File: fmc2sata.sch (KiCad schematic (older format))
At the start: 40 parts, among them J1 ASP-134488-01, J2 1-2199230-6, J3 te-770829-1, U1 TPS565208, U2 TPS565208, Y1 AX3DAF1-150.0000

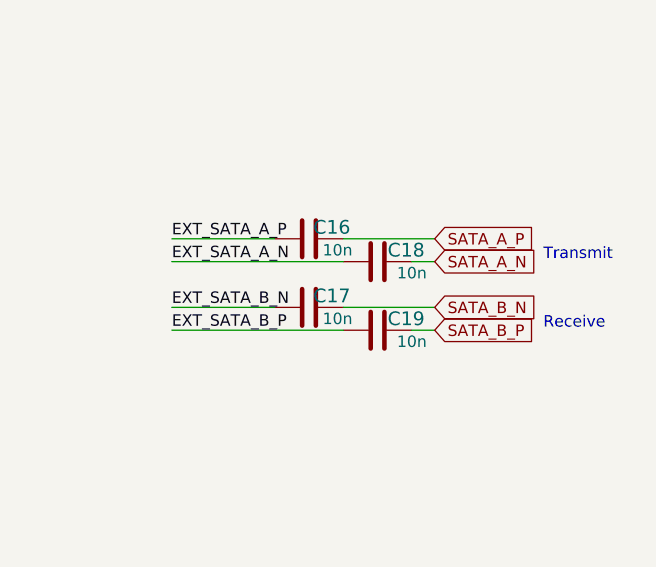
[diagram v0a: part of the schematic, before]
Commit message: Add board fastening holes
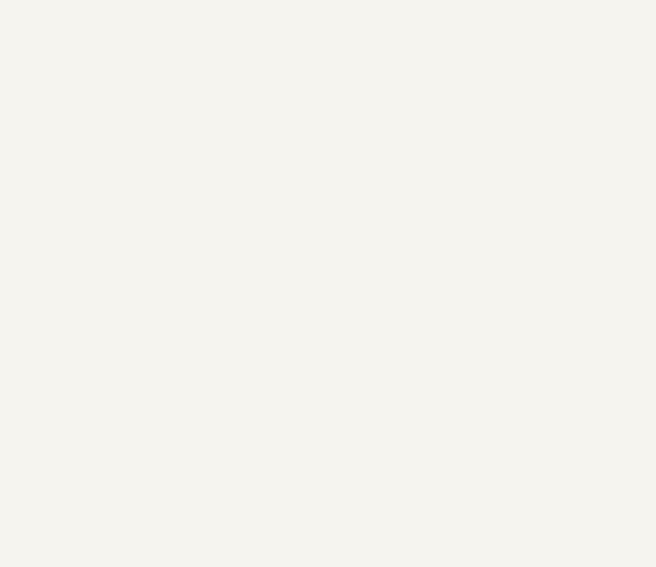
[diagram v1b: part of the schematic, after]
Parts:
- removed C16, C17, C18, C19: C_10n_0402, antmicro-footprints:0402-cap, symbol antmicroCapacitors0402:C_10n_0402
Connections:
- net labels removed: EXT_SATA_A_N, EXT_SATA_A_P, EXT_SATA_B_N, EXT_SATA_B_P
- wire segments 268 -> 260
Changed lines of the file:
@@
 Text Label 10650 4525 0    50   ~ 0
 M2_SATA_B_P
-Text GLabel 14900 5550 2    50   Input ~ 0
-SATA_B_P
-Text GLabel 14900 5450 2    50   Input ~ 0
-SATA_B_N
-Text Notes 15375 5550 0    50   ~ 0
-Receive
-Wire Wire Line
-	14200 5450 13750 5450
-Wire Wire Line
-	14800 5550 14900 5550
-Wire Wire Line
-	14500 5450 14900 5450
-Wire Wire Line
-	13750 5550 14500 5550
-$Comp
-L antmicroCapacitors0402:C_10n_0402 C19
-U 1 1 603C8A00
-P 14650 5550
-F 0 "C19" V 14600 5675 60  0000 C CNN
-F 1 "C_10n_0402" H 14650 5400 60  0001 C CNN
-F 2 "antmicro-footprints:0402-cap" H 14850 5750 60  0001 L CNN
-F 3 "" H 14650 5550 50  0001 C CNN
-F 4 "AVX" H 14850 5950 60  0001 L CNN "Manufacturer"
-F 5 "04025G103ZAT2A" H 14850 5850 60  0001 L CNN "MPN"
-F 6 "10n" V 14700 5700 50  0000 C CNN "Val"
-	1    14650 5550
-	0    1    1    0
-$EndComp
-$Comp
-L antmicroCapacitors0402:C_10n_0402 C17
-U 1 1 603C8A09
-P 14350 5450
-F 0 "C17" V 14300 5550 60  0000 C CNN
-F 1 "C_10n_0402" H 14350 5300 60  0001 C CNN
-F 2 "antmicro-footprints:0402-cap" H 14550 5650 60  0001 L CNN
-F 3 "" H 14350 5450 50  0001 C CNN
-F 4 "AVX" H 14550 5850 60  0001 L CNN "Manufacturer"
-F 5 "04025G103ZAT2A" H 14550 5750 60  0001 L CNN "MPN"
-F 6 "10n" V 14400 5575 50  0000 C CNN "Val"
-	1    14350 5450
-	0    1    1    0
-$EndComp
-Text Notes 15375 5250 0    50   ~ 0
-Transmit
-Wire Wire Line
-	14800 5250 14900 5250
-Wire Wire Line
-	14500 5150 14900 5150
-Wire Wire Line
-	13750 5250 14500 5250
-$Comp
-L antmicroCapacitors0402:C_10n_0402 C18
-U 1 1 603C8A16
-P 14650 5250
-F 0 "C18" V 14600 5375 60  0000 C CNN
-F 1 "C_10n_0402" H 14650 5100 60  0001 C CNN
-F 2 "antmicro-footprints:0402-cap" H 14850 5450 60  0001 L CNN
-F 3 "" H 14650 5250 50  0001 C CNN
-F 4 "AVX" H 14850 5650 60  0001 L CNN "Manufacturer"
-F 5 "04025G103ZAT2A" H 14850 5550 60  0001 L CNN "MPN"
-F 6 "10n" V 14700 5400 50  0000 C CNN "Val"
-	1    14650 5250
-	0    1    1    0
-$EndComp
-$Comp
-L antmicroCapacitors0402:C_10n_0402 C16
-U 1 1 603C8A1F
-P 14350 5150
-F 0 "C16" V 14300 5250 60  0000 C CNN
-F 1 "C_10n_0402" H 14350 5000 60  0001 C CNN
-F 2 "antmicro-footprints:0402-cap" H 14550 5350 60  0001 L CNN
-F 3 "" H 14350 5150 50  0001 C CNN
-F 4 "AVX" H 14550 5550 60  0001 L CNN "Manufacturer"
-F 5 "04025G103ZAT2A" H 14550 5450 60  0001 L CNN "MPN"
-F 6 "10n" V 14400 5275 50  0000 C CNN "Val"
-	1    14350 5150
-	0    1    1    0
-$EndComp
-Text GLabel 14900 5150 2    50   Input ~ 0
-SATA_A_P
-Text GLabel 14900 5250 2    50   Input ~ 0
-SATA_A_N
-Wire Wire Line
-	13750 5150 14200 5150
-Text Label 13750 5150 0    50   ~ 0
-EXT_SATA_A_P
-Text Label 13750 5250 0    50   ~ 0
-EXT_SATA_A_N
-Text Label 13750 5450 0    50   ~ 0
-EXT_SATA_B_N
-Text Label 13750 5550 0    50   ~ 0
-EXT_SATA_B_P
 $Comp
 L antmicroPCConnectors:te-770829-1 J3

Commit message: Add second M.2 mouting stud
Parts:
- added N1: antmicro_logo, antmicro-footprints:antmicro-logo, symbol antmicroMechanicalParts:antmicro_logo
- added N2: oshw_logo, antmicro-footprints:oshw-logo, symbol antmicroMechanicalParts:oshw_logo
- added SP2: 9774025151, antmicro-footprints:9774025151, symbol antmicroMechanicalParts:9774025151
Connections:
- wire segments 260 -> 262
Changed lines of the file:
@@
 L power:GND #PWR01
 U 1 1 6009AC9F
-P 9325 7650
-F 0 "#PWR01" H 9325 7400 50  0001 C CNN
-F 1 "GND" H 9330 7477 50  0000 C CNN
-F 2 "" H 9325 7650 50  0001 C CNN
-F 3 "" H 9325 7650 50  0001 C CNN
-	1    9325 7650
+P 9325 7875
+F 0 "#PWR01" H 9325 7625 50  0001 C CNN
+F 1 "GND" H 9330 7702 50  0000 C CNN
+F 2 "" H 9325 7875 50  0001 C CNN
+F 3 "" H 9325 7875 50  0001 C CNN
+	1    9325 7875
 	1    0    0    -1
 $EndComp
@@
 	9400 7500 9325 7500
 Wire Wire Line
-	9325 7500 9325 7650
+	9325 7500 9325 7825
 Text Notes 13700 2425 0    79   ~ 16
 2.5" Drive Power Connector
@@
 Wire Wire Line
 	13450 3300 13450 3150
+$Comp
+L antmicroMechanicalParts:9774025151 SP2
+U 1 1 601E6B56
+P 9600 7825
+F 0 "SP2" H 9730 7878 60  0000 L CNN
+F 1 "9774025151" H 9730 7772 60  0000 L CNN
+F 2 "antmicro-footprints:9774025151" H 9600 7825 60  0001 C CNN
+F 3 "" H 9600 7825 60  0001 C CNN
+F 4 "Wurth Elektronik" H 9600 7825 50  0001 C CNN "Manufacturer"
+F 5 "9774025151" H 9600 7825 50  0001 C CNN "MPN"
+	1    9600 7825
+	1    0    0    -1
+$EndComp
+Wire Wire Line
+	9400 7825 9325 7825
+Connection ~ 9325 7825
+Wire Wire Line
+	9325 7825 9325 7875
+$Comp
+L antmicroMechanicalParts:oshw_logo N2
+U 1 1 6021D7FF
+P 15225 9575
+F 0 "N2" H 15419 9578 50  0000 L CNN
+F 1 "oshw_logo" H 15419 9487 50  0000 L CNN
+F 2 "antmicro-footprints:oshw-logo" H 15245 9335 50  0001 C CNN
+F 3 "" H 15225 9575 50  0001 C CNN
+	1    15225 9575
+	1    0    0    -1
+$EndComp
+$Comp
+L antmicroMechanicalParts:antmicro_logo N1
+U 1 1 6021EA88
+P 14325 9700
+F 0 "N1" H 14539 9793 50  0000 L CNN
+F 1 "antmicro_logo" H 14539 9702 50  0000 L CNN
+F 2 "antmicro-footprints:antmicro-logo" H 14225 9950 50  0001 C CNN
+F 3 "" H 14325 10050 50  0001 C CNN
+	1    14325 9700
+	1    0    0    -1
+$EndComp
 $EndSCHEMATC

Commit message: Add PWR indicators
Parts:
- removed R10: R_1k_0402, antmicro-footprints:0402-res, symbol antmicroResistors0402:R_1k_0402
- added D2: LTST-C191KRKT, antmicro-footprints:LED_0603, symbol antmicroLEDIndicationDiscrete:LTST-C191KRKT
- added D3, D4, D5: KP-1608CGCK, antmicro-footprints:LED_0603, symbol antmicroLEDIndicationDiscrete:KP-1608CGCK
- added Q1, Q2, Q4: BSS138APW, antmicro-footprints:SC70-3, symbol antmicroTransistorsFETsMOSFETsSingle:BSS138APW
- added Q3: DMG2305UX-13, antmicro-footprints:SOT-23-3, symbol antmicroTransistorsFETsMOSFETsSingle:DMG2305UX-13
- added R10, R14, R15, R20: R_10k_0402, antmicro-footprints:0402-res, symbol antmicroResistors0402:R_10k_0402
- added R12, R13, R21, R22: R_0R_0402, antmicro-footprints:0402-res, symbol antmicroResistors0402:R_0R_0402
- added R16, R17, R18, R19: R_330R_0402, antmicro-footprints:0402-res, symbol antmicroResistors0402:R_330R_0402
- N1: footprint antmicro-footprints:antmicro-logo -> antmicro-footprints:antmicro-logo_scaled_20mm
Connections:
- net labels added: JTAG_TDI, JTAG_TDO, PRSNT, VCC_IO
- wire segments 262 -> 295
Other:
- note added: "JTAG loop"
- note added: "LED indicators"
- note added: "Signage"
- note added: "VADJ"
- moved on the sheet: C1, C10, C11, C12, C13, C14, C15, C2, C3, C4, C5, C6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

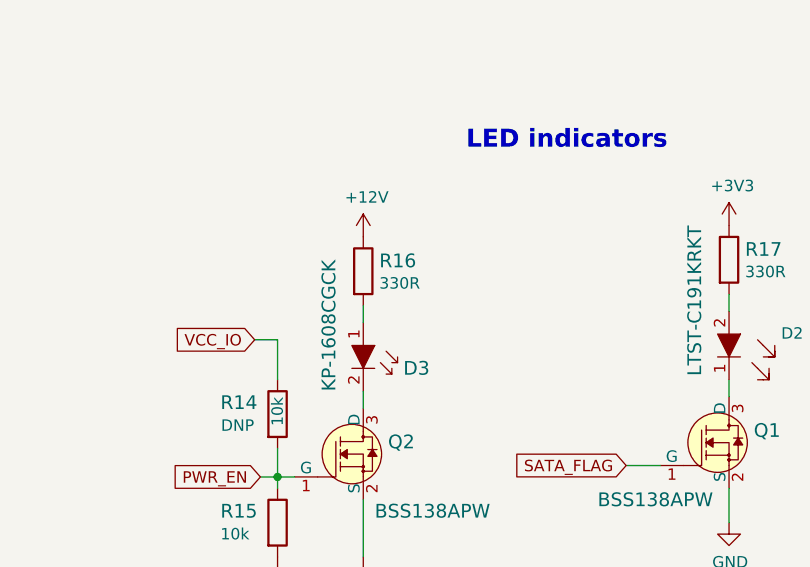
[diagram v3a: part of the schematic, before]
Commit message: Update compoent placement
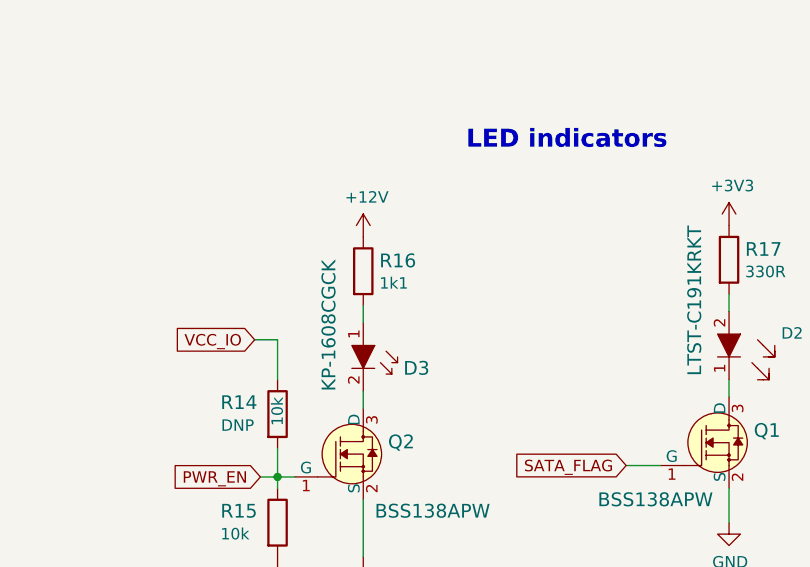
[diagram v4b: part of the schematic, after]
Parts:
- removed R16: R_330R_0402, antmicro-footprints:0402-res, symbol antmicroResistors0402:R_330R_0402
- added R16: R_1k1_0402, antmicro-footprints:0402-res, symbol antmicroResistors0402:R_1k1_0402
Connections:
- net +12V: now also R16.1
- net at D3.1: now also R16.2
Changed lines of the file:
@@
 Wire Wire Line
 	12350 6825 12350 7075
-$Comp
-L antmicroResistors0402:R_330R_0402 R16
-U 1 1 6042387E
-P 12350 5825
-F 0 "R16" V 12305 5895 60  0000 L CNN
-F 1 "R_330R_0402" H 12350 5675 60  0001 C CNN
-F 2 "antmicro-footprints:0402-res" H 12550 6025 60  0001 L CNN
-F 3 "" H 12350 5825 50  0001 C CNN
-F 4 "MULTICOMP" H 12550 6225 60  0001 L CNN "Manufacturer"
-F 5 "MCMR04X3300FTL" H 12550 6125 60  0001 L CNN "MPN"
-F 6 "330R" V 12403 5895 50  0000 L CNN "Val"
-	1    12350 5825
-	0    1    1    0
-$EndComp
 Wire Wire Line
 	12350 5975 12350 6050
@@
 Text Notes 3100 5575 0    39   ~ 0
 JTAG loop
+$Comp
+L antmicroResistors0402:R_1k1_0402 R16
+U 1 1 608DD822
+P 12350 5825
+F 0 "R16" V 12305 5895 60  0000 L CNN
+F 1 "R_1k1_0402" H 12350 5675 60  0001 C CNN
+F 2 "antmicro-footprints:0402-res" H 12550 6025 60  0001 L CNN
+F 3 "" H 12350 5825 50  0001 C CNN
+F 4 "PANASONIC_ELECTRONIC_COMPONENTS" H 12550 6225 60  0001 L CNN "Manufacturer"
+F 5 "ERJ2RKF1101X" H 12550 6125 60  0001 L CNN "MPN"
+F 6 "1k1" V 12403 5895 50  0000 L CNN "Val"
+	1    12350 5825
+	0    1    1    0
+$EndComp
 $EndSCHEMATC

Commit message: Component cleanup
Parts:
- C1, C2, C6, C7: footprint antmicro-footprints:0603-cap -> fmc2sata-footprints:0603-cap; symbol antmicroCapacitors0603:C_10u_25V_0603 -> fmc2sata:C_10u_25V_0603
- C10, C4, C5, C9: footprint antmicro-footprints:0805-cap -> fmc2sata-footprints:0805-cap; symbol antmicroCapacitorsmisc:C_22u_0805_10V -> fmc2sata:C_22u_0805_10V
- C3, C8: footprint antmicro-footprints:0603-cap -> fmc2sata-footprints:0603-cap; symbol antmicroCapacitors0603:C_100n_0603 -> fmc2sata:C_100n_0603
- D1, D3, D4, D5: footprint antmicro-footprints:LED_0603 -> fmc2sata-footprints:LED_0603; symbol antmicroLEDIndicationDiscrete:KP-1608CGCK -> fmc2sata:KP-1608CGCK
- D2: footprint antmicro-footprints:LED_0603 -> fmc2sata-footprints:LED_0603; symbol antmicroLEDIndicationDiscrete:LTST-C191KRKT -> fmc2sata:LTST-C191KRKT
- J1: footprint antmicro-footprints:ASP-134488-01 -> fmc2sata-footprints:ASP-134488-01; symbol antmicroFMCConnectors:ASP-134488-01 -> fmc2sata:ASP-134488-01
- J2: footprint antmicro-footprints:1-2199230-6 -> fmc2sata-footprints:1-2199230-6; symbol antmicroPciConnectors:1-2199230-6 -> fmc2sata:1-2199230-6
- J3: footprint antmicro-footprints:te-770829-1 -> fmc2sata-footprints:te-770829-1; symbol antmicroPCConnectors:te-770829-1 -> fmc2sata:te-770829-1
- L1: footprint antmicro-footprints:WE_74437336022 -> fmc2sata-footprints:WE_74437336022; symbol antmicroFixedInductors:WE_74437336022 -> fmc2sata:WE_74437336022
- L2: footprint antmicro-footprints:WE_74437336033 -> fmc2sata-footprints:WE_74437336033; symbol antmicroFixedInductors:WE_74437336033 -> fmc2sata:WE_74437336033
- N1: footprint antmicro-footprints:antmicro-logo_scaled_20mm -> fmc2sata-footprints:antmicro-logo_scaled_20mm; symbol antmicroMechanicalParts:antmicro_logo -> fmc2sata:antmicro_logo
- N2: footprint antmicro-footprints:oshw-logo -> fmc2sata-footprints:oshw-logo; symbol antmicroMechanicalParts:oshw_logo -> fmc2sata:oshw_logo
- Q1, Q2, Q4: footprint antmicro-footprints:SC70-3 -> fmc2sata-footprints:SC70-3; symbol antmicroTransistorsFETsMOSFETsSingle:BSS138APW -> fmc2sata:BSS138APW
- Q3: footprint antmicro-footprints:SOT-23-3 -> fmc2sata-footprints:SOT-23-3; symbol antmicroTransistorsFETsMOSFETsSingle:DMG2305UX-13 -> fmc2sata:DMG2305UX-13
- R1: footprint antmicro-footprints:0402-res -> fmc2sata-footprints:0402-res; symbol antmicroResistors0402:R_33k2_0402 -> fmc2sata:R_33k2_0402
- R11: footprint antmicro-footprints:0402-res -> fmc2sata-footprints:0402-res; symbol antmicroResistors0402:R_100R_0402 -> fmc2sata:R_100R_0402
- R12, R13, R21, R22, R3, R7, R9: footprint antmicro-footprints:0402-res -> fmc2sata-footprints:0402-res; symbol antmicroResistors0402:R_0R_0402 -> fmc2sata:R_0R_0402
- R17, R18, R19, R6: footprint antmicro-footprints:0402-res -> fmc2sata-footprints:0402-res; symbol antmicroResistors0402:R_330R_0402 -> fmc2sata:R_330R_0402
- R4: footprint antmicro-footprints:0402-res -> fmc2sata-footprints:0402-res; symbol antmicroResistors0402:R_54k9_0402 -> fmc2sata:R_54k9_0402
- SP1, SP2: footprint antmicro-footprints:9774025151 -> fmc2sata-footprints:9774025151; symbol antmicroMechanicalParts:9774025151 -> fmc2sata:9774025151
- U1, U2: footprint antmicro-footprints:SOT-23-6 -> fmc2sata-footprints:SOT-23-6; symbol antmicroPMICVoltageRegulatorsDCDCSwitchingRegulators:TPS565208 -> fmc2sata:TPS565208
- Y1: footprint antmicro-footprints:AX3DAF1 -> fmc2sata-footprints:AX3DAF1; symbol antmicroOscillators:AX3DAF1-150.0000 -> fmc2sata:AX3DAF1-150.0000

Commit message: Update local libraries
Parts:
- C11: footprint antmicro-footprints:0402-cap -> fmc2sata-footprints:0402-cap; symbol antmicroCapacitors0402:C_100n_0402 -> fmc2sata:C_100n_0402
- C12, C13, C14, C15: footprint antmicro-footprints:0402-cap -> fmc2sata-footprints:0402-cap; symbol antmicroCapacitors0402:C_10n_0402 -> fmc2sata:C_10n_0402
- R10, R14, R15, R2, R20, R5, R8: footprint antmicro-footprints:0402-res -> fmc2sata-footprints:0402-res; symbol antmicroResistors0402:R_10k_0402 -> fmc2sata:R_10k_0402
- R16: footprint antmicro-footprints:0402-res -> fmc2sata-footprints:0402-res; symbol antmicroResistors0402:R_1k1_0402 -> fmc2sata:R_1k1_0402
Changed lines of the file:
@@
 Connection ~ 9925 3950
 $Comp
-L antmicroResistors0402:R_10k_0402 R8
+L fmc2sata:R_10k_0402 R8
 U 1 1 60081456
 P 10125 3025
 F 0 "R8" V 10080 3095 60  0000 L CNN
 F 1 "R_10k_0402" H 10125 2875 60  0001 C CNN
-F 2 "antmicro-footprints:0402-res" H 10325 3225 60  0001 L CNN
+F 2 "fmc2sata-footprints:0402-res" H 10325 3225 60  0001 L CNN
 F 3 "" H 10125 3025 50  0001 C CNN
 F 4 "VISHAY" H 10325 3425 60  0001 L CNN "Manufacturer"
@@
 $EndComp
 $Comp
-L antmicroResistors0402:R_10k_0402 R2
+L fmc2sata:R_10k_0402 R2
 U 1 1 6043BD03
 P 3600 9925
 F 0 "R2" V 3555 9995 60  0000 L CNN
 F 1 "R_10k_0402" H 3600 9775 60  0001 C CNN
-F 2 "antmicro-footprints:0402-res" H 3800 10125 60  0001 L CNN
+F 2 "fmc2sata-footprints:0402-res" H 3800 10125 60  0001 L CNN
 F 3 "" H 3600 9925 50  0001 C CNN
 F 4 "VISHAY" H 3800 10325 60  0001 L CNN "Manufacturer"
@@
 $EndComp
 $Comp
-L antmicroResistors0402:R_10k_0402 R5
+L fmc2sata:R_10k_0402 R5
 U 1 1 604BD594
 P 7900 9925
 F 0 "R5" V 7855 9995 60  0000 L CNN
 F 1 "R_10k_0402" H 7900 9775 60  0001 C CNN
-F 2 "antmicro-footprints:0402-res" H 8100 10125 60  0001 L CNN
+F 2 "fmc2sata-footprints:0402-res" H 8100 10125 60  0001 L CNN
 F 3 "" H 7900 9925 50  0001 C CNN
 F 4 "VISHAY" H 8100 10325 60  0001 L CNN "Manufacturer"
@@
 	10625 9675 10625 9775
 $Comp
-L antmicroCapacitors0402:C_100n_0402 C11
+L fmc2sata:C_100n_0402 C11
 U 1 1 601CBF20
 P 10050 9600
 F 0 "C11" H 9725 9675 60  0000 L CNN
 F 1 "C_100n_0402" H 10050 9450 60  0001 C CNN
-F 2 "antmicro-footprints:0402-cap" H 10250 9800 60  0001 L CNN
+F 2 "fmc2sata-footprints:0402-cap" H 10250 9800 60  0001 L CNN
 F 3 "" H 10050 9600 50  0001 C CNN
 F 4 "Walsin" H 10250 10000 60  0001 L CNN "Manufacturer"
@@
 	9750 4450 10750 4450
 $Comp
-L antmicroCapacitors0402:C_10n_0402 C15
+L fmc2sata:C_10n_0402 C15
 U 1 1 60364053
 P 10900 4450
 F 0 "C15" V 10850 4575 60  0000 C CNN
 F 1 "C_10n_0402" H 10900 4300 60  0001 C CNN
-F 2 "antmicro-footprints:0402-cap" H 11100 4650 60  0001 L CNN
+F 2 "fmc2sata-footprints:0402-cap" H 11100 4650 60  0001 L CNN
 F 3 "" H 10900 4450 50  0001 C CNN
 F 4 "AVX" H 11100 4850 60  0001 L CNN "Manufacturer"
@@
 $EndComp
 $Comp
-L antmicroCapacitors0402:C_10n_0402 C13
+L fmc2sata:C_10n_0402 C13
 U 1 1 6036405C
 P 10600 4350
 F 0 "C13" V 10550 4450 60  0000 C CNN
 F 1 "C_10n_0402" H 10600 4200 60  0001 C CNN
-F 2 "antmicro-footprints:0402-cap" H 10800 4550 60  0001 L CNN
+F 2 "fmc2sata-footprints:0402-cap" H 10800 4550 60  0001 L CNN
 F 3 "" H 10600 4350 50  0001 C CNN
 F 4 "AVX" H 10800 4750 60  0001 L CNN "Manufacturer"
@@
 	9750 4150 10750 4150
 $Comp
-L antmicroCapacitors0402:C_10n_0402 C14
+L fmc2sata:C_10n_0402 C14
 U 1 1 60364069
 P 10900 4150
 F 0 "C14" V 10850 4275 60  0000 C CNN
 F 1 "C_10n_0402" H 10900 4000 60  0001 C CNN
-F 2 "antmicro-footprints:0402-cap" H 11100 4350 60  0001 L CNN
+F 2 "fmc2sata-footprints:0402-cap" H 11100 4350 60  0001 L CNN
 F 3 "" H 10900 4150 50  0001 C CNN
 F 4 "AVX" H 11100 4550 60  0001 L CNN "Manufacturer"
@@
 $EndComp
 $Comp
-L antmicroCapacitors0402:C_10n_0402 C12
+L fmc2sata:C_10n_0402 C12
 U 1 1 60364072
 P 10600 4050
 F 0 "C12" V 10550 4150 60  0000 C CNN
 F 1 "C_10n_0402" H 10600 3900 60  0001 C CNN
-F 2 "antmicro-footprints:0402-cap" H 10800 4250 60  0001 L CNN
+F 2 "fmc2sata-footprints:0402-cap" H 10800 4250 60  0001 L CNN
 F 3 "" H 10600 4050 50  0001 C CNN
 F 4 "AVX" H 10800 4450 60  0001 L CNN "Manufacturer"
@@
 VCC_IO
 $Comp
-L antmicroResistors0402:R_10k_0402 R14
+L fmc2sata:R_10k_0402 R14
 U 1 1 6044FD7D
 P 11975 6450
 F 0 "R14" V 11925 6200 60  0000 L CNN
 F 1 "R_10k_0402" H 11975 6300 60  0001 C CNN
-F 2 "antmicro-footprints:0402-res" H 12175 6650 60  0001 L CNN
+F 2 "fmc2sata-footprints:0402-res" H 12175 6650 60  0001 L CNN
 F 3 "" H 11975 6450 50  0001 C CNN
 F 4 "VISHAY" H 12175 6850 60  0001 L CNN "Manufacturer"
@@
 	11975 6725 12050 6725
 $Comp
-L antmicroResistors0402:R_10k_0402 R15
+L fmc2sata:R_10k_0402 R15
 U 1 1 6047C421
 P 11975 6925
 F 0 "R15" V 11925 6675 60  0000 L CNN
 F 1 "R_10k_0402" H 11975 6775 60  0001 C CNN
-F 2 "antmicro-footprints:0402-res" H 12175 7125 60  0001 L CNN
+F 2 "fmc2sata-footprints:0402-res" H 12175 7125 60  0001 L CNN
 F 3 "" H 11975 6925 50  0001 C CNN
 F 4 "VISHAY" H 12175 7325 60  0001 L CNN "Manufacturer"
@@
 $EndComp
 $Comp
-L antmicroResistors0402:R_10k_0402 R10
+L fmc2sata:R_10k_0402 R10
 U 1 1 604C52E8
 P 10475 9575
 F 0 "R10" V 10430 9645 60  0000 L CNN
 F 1 "R_10k_0402" H 10475 9425 60  0001 C CNN
-F 2 "antmicro-footprints:0402-res" H 10675 9775 60  0001 L CNN
+F 2 "fmc2sata-footprints:0402-res" H 10675 9775 60  0001 L CNN
 F 3 "" H 10475 9575 50  0001 C CNN
 F 4 "VISHAY" H 10675 9975 60  0001 L CNN "Manufacturer"
@@
 $EndComp
 $Comp
-L antmicroResistors0402:R_10k_0402 R20
+L fmc2sata:R_10k_0402 R20
 U 1 1 60747085
 P 13300 3475
 F 0 "R20" V 13250 3225 60  0000 L CNN
 F 1 "R_10k_0402" H 13300 3325 60  0001 C CNN
-F 2 "antmicro-footprints:0402-res" H 13500 3675 60  0001 L CNN
+F 2 "fmc2sata-footprints:0402-res" H 13500 3675 60  0001 L CNN
 F 3 "" H 13300 3475 50  0001 C CNN
 F 4 "VISHAY" H 13500 3875 60  0001 L CNN "Manufacturer"
@@
 JTAG loop
 $Comp
-L antmicroResistors0402:R_1k1_0402 R16
+L fmc2sata:R_1k1_0402 R16
 U 1 1 608DD822
 P 12350 5825
 F 0 "R16" V 12305 5895 60  0000 L CNN
 F 1 "R_1k1_0402" H 12350 5675 60  0001 C CNN
-F 2 "antmicro-footprints:0402-res" H 12550 6025 60  0001 L CNN
+F 2 "fmc2sata-footprints:0402-res" H 12550 6025 60  0001 L CNN
 F 3 "" H 12350 5825 50  0001 C CNN
 F 4 "PANASONIC_ELECTRONIC_COMPONENTS" H 12550 6225 60  0001 L CNN "Manufacturer"
